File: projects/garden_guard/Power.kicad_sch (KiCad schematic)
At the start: 46 parts, among them IC1 ACPL-227-50CE, IC2 INA226AQDGSRQ1, IC3 INA226AQDGSRQ1, J8 USB_C_Receptacle_USB2.0, U7 Ag5810, U8 TPS2121RUXR, U9 MAX20408AFOF

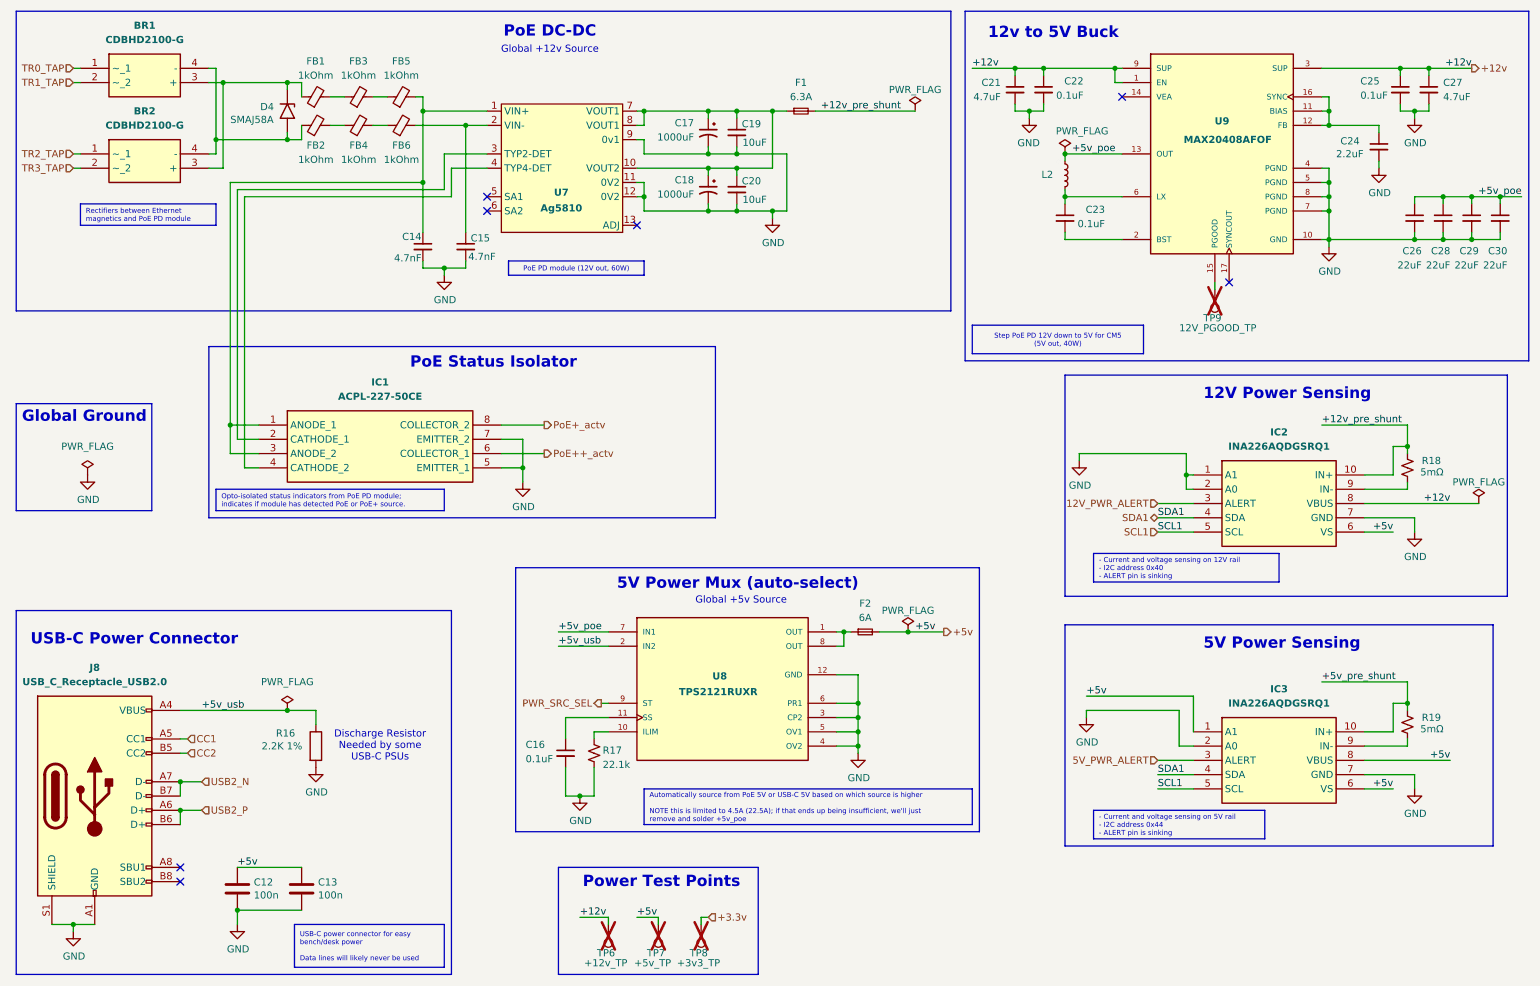
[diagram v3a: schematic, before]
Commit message: - Find part numbers for CM5 parts - Minor CM5 symbol, footprint adjustments - Move to uniform small resistor and capacitor symbols - Add *lck to .gitignore
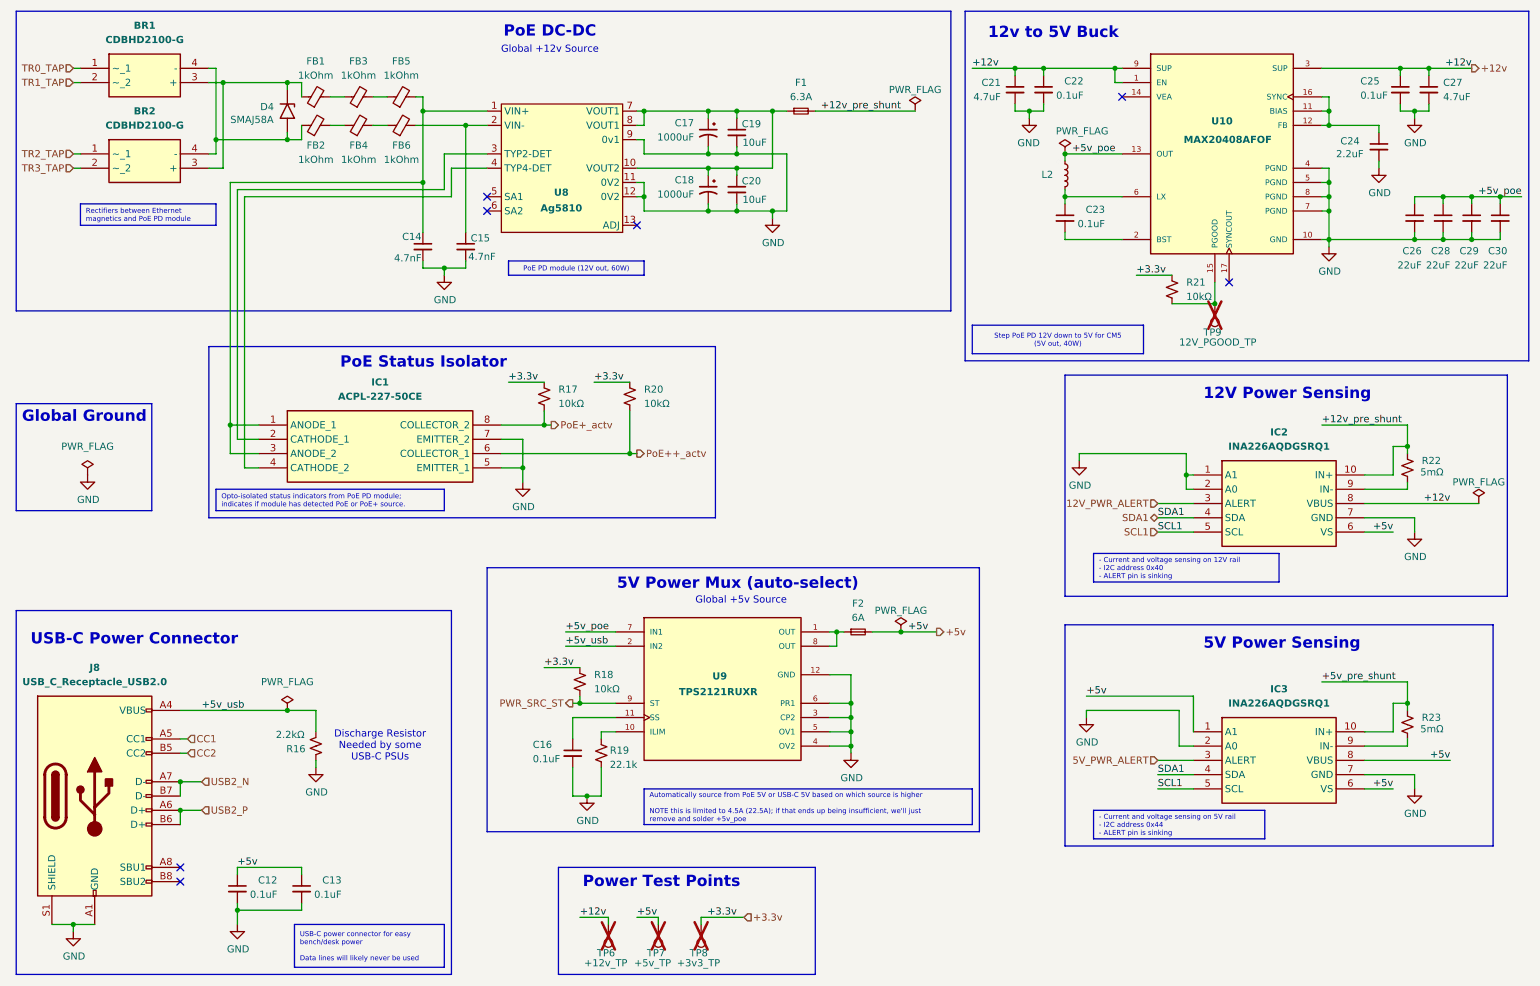
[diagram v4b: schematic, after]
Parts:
- removed C12, C13: 100n, Capacitor_SMD:C_0402_1005Metric, symbol Device:C
- removed R16: 2.2K 1%, Resistor_SMD:R_0402_1005Metric, symbol Device:R
- added C12, C13: 0.1uF, Resistor_SMD:R_0603_1608Metric, symbol Device:C_Small
- added R16: 2.2kΩ, Resistor_SMD:R_0201_0603Metric, symbol Device:R_Small_US
- added R17, R18, R20, R21: 10kΩ, Resistor_SMD:R_0603_1608Metric, symbol Device:R_Small_US
- BR1, BR2: MPN (none) -> CDBHD2100-G; Mfr (none) -> Comchip Technology
- C16, C22, C23, C25: Mfr (none) -> KEMET
- IC1: MPN (none) -> ACPL-227-50CE; Mfr (none) -> Broadcom Limited
- IC2, IC3: MPN (none) -> INA226AQDGSRQ1; Mfr (none) -> Texas Instruments
- J8: MPN (none) -> UJ20-C-H-G-SMT-1-P16-TR; Mfr (none) -> Same Sky
- U10: renamed from U9; MPN (none) -> MAX20408AFOF/VY+; Mfr (none) -> Analog Devices
- U8: renamed from U7; MPN (none) -> AG5810; Mfr (none) -> Silvertel
- U9: renamed from U8; MPN (none) -> TPS2121RUXR; Mfr (none) -> Texas Instruments
- renumbered R17 to R19, R18 to R22, R19 to R23
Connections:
- net +3.3v: now also R17.1, R18.1, R20.1, R21.1
- net +5v: now also C12.1, C13.1
- net +5v_usb: now also R16.1
- net GND: now also C12.2, C13.2, R16.2
- net PoE++_actv: now also R20.2
- net PoE+_actv: now also R17.2
- net at TP9.1, U10.15 (PGOOD): now also R21.2
- net PWR_SRC_SEL renamed PWR_SRC_ST
- net PWR_SRC_ST: now also R18.2
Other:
- moved on the sheet: C16, F2, R19, TP9

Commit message: - Assign 3D models to lingering footprints lacking them - Start playing with board layout - Move CM5 library files from project to components dir
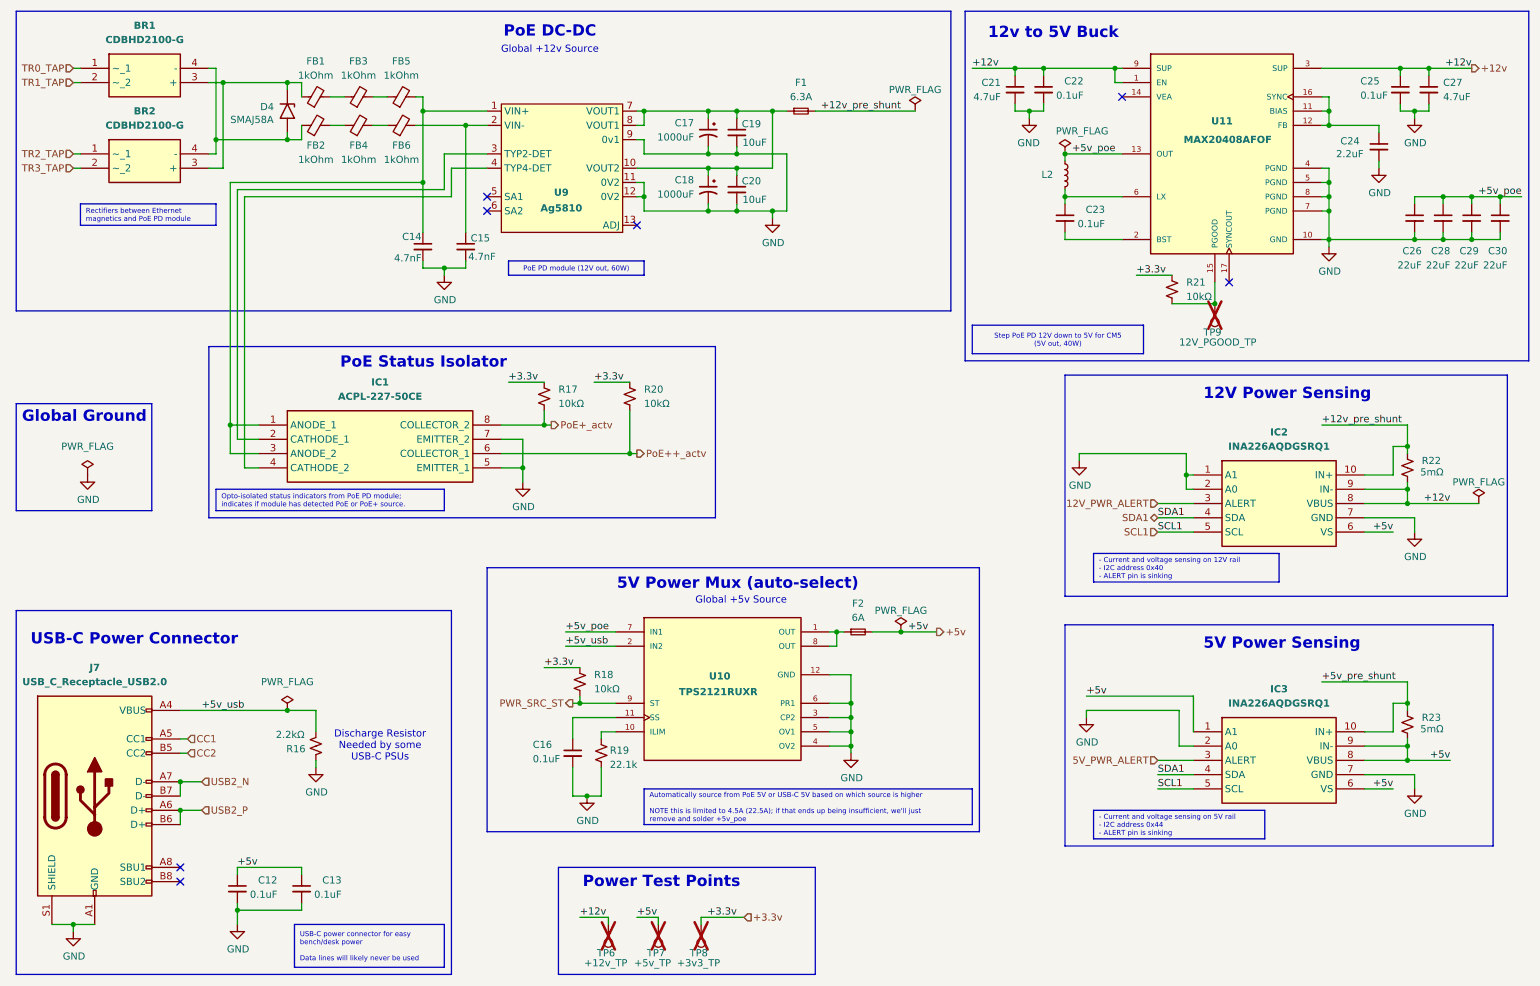
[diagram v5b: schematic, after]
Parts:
- IC1: footprint Custom_PoE:SOIC127P700X220-8N -> Custom_PoE:ACPL-227-50CE
- renumbered J8 to J7, U9 to U10, U10 to U11, U8 to U9
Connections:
- net +12v: now also IC2.9 (IN-), R22.2
- net +5v: now also IC3.9 (IN-), R23.2
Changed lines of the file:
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@@
 	)
 	(junction
+		(at 261.62 144.78)
+		(diameter 0)
+		(color 0 0 0 0)
+	)
+	(junction
 		(at 86.36 31.75)
 		(diameter 0)
@@
 	)
 	(junction
+		(at 261.62 99.06)
+		(diameter 0)
+		(color 0 0 0 0)
+	)
+	(junction
 		(at 260.35 24.13)
 		(diameter 0)
@@
 	)
 	(junction
+		(at 261.62 101.6)
+		(diameter 0)
+		(color 0 0 0 0)
+	)
+	(junction
 		(at 24.13 176.53)
 		(diameter 0)
@@
 	)
 	(junction
+		(at 261.62 147.32)
+		(diameter 0)
+		(color 0 0 0 0)
+	)
+	(junction
 		(at 261.62 137.16)
 		(diameter 0)
@@
 	(wire
 		(pts
+			(xy 261.62 99.06) (xy 261.62 101.6)
+		)
+		(stroke
+			(width 0)
+			(type default)
+		)
+	)
+	(wire
+		(pts
 			(xy 267.97 46.99) (xy 267.97 48.26)
 		)
@@
 	(wire
 		(pts
-			(xy 254 101.6) (xy 274.32 101.6)
+			(xy 254 101.6) (xy 261.62 101.6)
 		)
 		(stroke
@@
 	(wire
 		(pts
+			(xy 261.62 101.6) (xy 274.32 101.6)
+		)
+		(stroke
+			(width 0)
+			(type default)
+		)
+	)
+	(wire
+		(pts
 			(xy 49.53 36.83) (xy 62.23 36.83)
 		)
@@
 	(wire
 		(pts
+			(xy 261.62 144.78) (xy 261.62 147.32)
+		)
+		(stroke
+			(width 0)
+			(type default)
+		)
+	)
+	(wire
+		(pts
 			(xy 166.37 124.46) (xy 171.45 124.46)
 		)
@@
 	(wire
 		(pts
-			(xy 254 147.32) (xy 269.24 147.32)
+			(xy 254 147.32) (xy 261.62 147.32)
 		)
 		(stroke
@@
 	(wire
 		(pts
+			(xy 261.62 147.32) (xy 269.24 147.32)
+		)
+		(stroke
+			(width 0)
+			(type default)
+		)
+	)
+	(wire
+		(pts
 			(xy 158.75 139.7) (xy 162.56 139.7)
 		)
@@
 			)
 		)
-		(property "Footprint" "Custom_PoE:SOIC127P700X220-8N"
+		(property "Footprint" "Custom_PoE:ACPL-227-50CE"
 			(at 96.52 182.55 0)
 			(effects
@@
 		(on_board yes)
 		(dnp no)
-		(property "Reference" "U10"
+		(property "Reference" "U11"
 			(at 228.6 33.528 0)
 			(effects
@@
 			(project ""
 				(path "/dcdac9d4-ef08-426f-b97c-7b9219501e71/446b5b12-2582-472d-9a1e-c1c7d43f42d1"
-					(reference "U10")
+					(reference "U11")
 					(unit 1)
 				)
@@
 		(on_board yes)
 		(dnp no)
-		(property "Reference" "U8"
+		(property "Reference" "U9"
 			(at 110.998 46.228 0)
 			(effects
@@
 			(project ""
 				(path "/dcdac9d4-ef08-426f-b97c-7b9219501e71/446b5b12-2582-472d-9a1e-c1c7d43f42d1"
-					(reference "U8")
+					(reference "U9")
 					(unit 1)
 				)
@@
 		(dnp no)
 		(fields_autoplaced yes)
-		(property "Reference" "J8"
+		(property "Reference" "J7"
 			(at 27.94 130.81 0)
 			(effects
@@
 			(project "garden_guard"
 				(path "/dcdac9d4-ef08-426f-b97c-7b9219501e71/446b5b12-2582-472d-9a1e-c1c7d43f42d1"
-					(reference "J8")
+					(reference "J7")
 					(unit 1)
 				)
@@
 		(on_board yes)
 		(dnp no)
-		(property "Reference" "U9"
+		(property "Reference" "U10"
 			(at 139.192 132.334 0)
 			(effects
@@
 			(project ""
 				(path "/dcdac9d4-ef08-426f-b97c-7b9219501e71/446b5b12-2582-472d-9a1e-c1c7d43f42d1"
-					(reference "U9")
+					(reference "U10")
 					(unit 1)
 				)

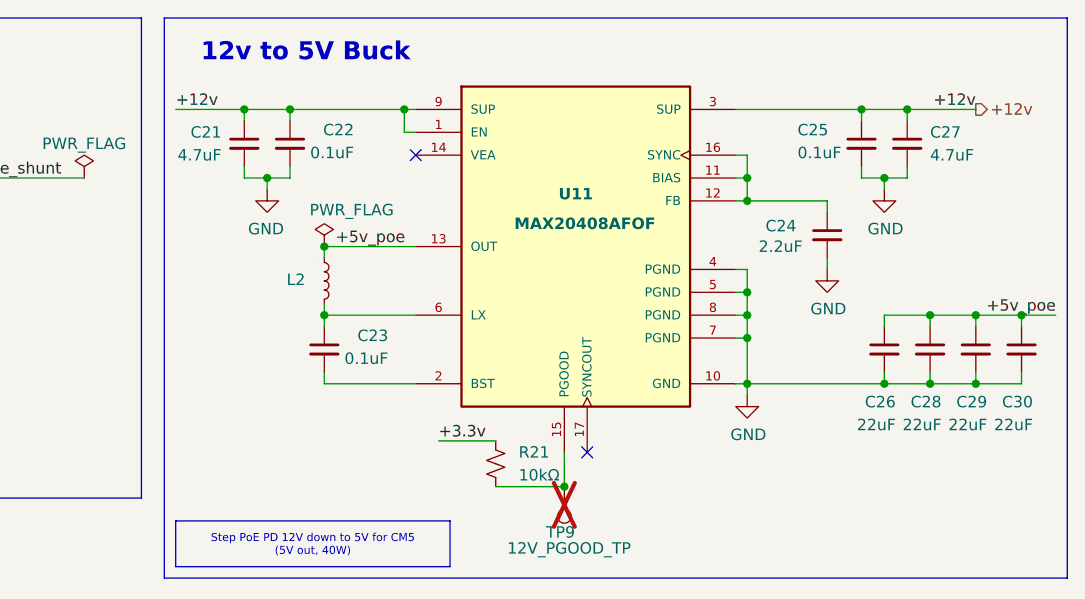
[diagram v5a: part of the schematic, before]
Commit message: 12V to 5V buck converter layout
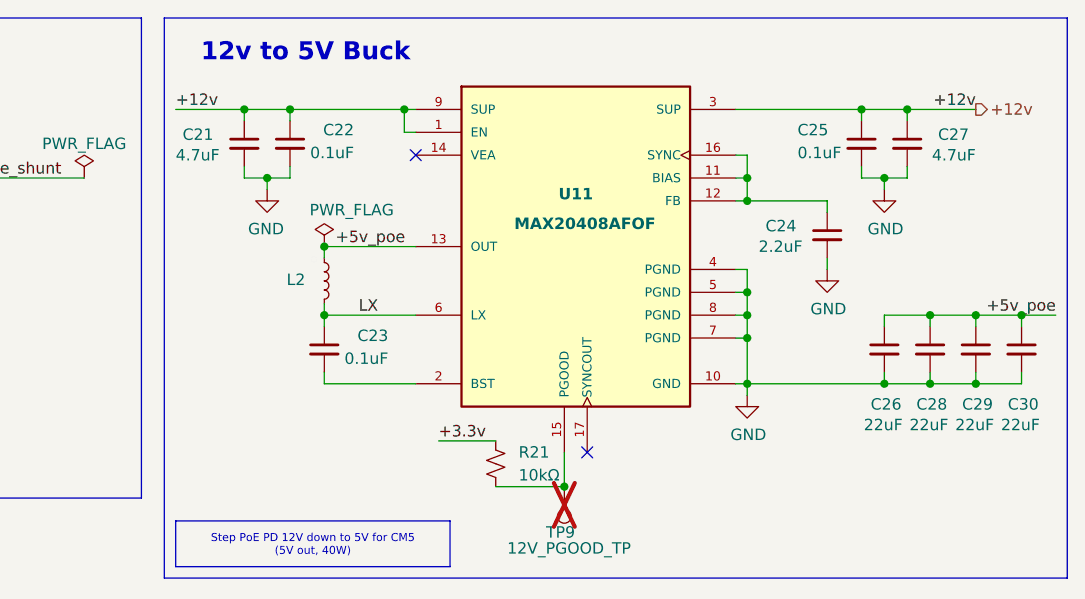
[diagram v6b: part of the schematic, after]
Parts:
- C21, C27: footprint Capacitor_SMD:C_0603_1608Metric -> Capacitor_SMD:C_0805_2012Metric; MPN GRM188R61E475KE11D -> GRM21BZ71E475KE15L; Max Temp (none) -> 125; Rating (none) -> None; Temp Coef (none) -> X7R; Tolerance (none) -> 10%; Voltage (none) -> 25V
- C22, C25: footprint Resistor_SMD:R_0603_1608Metric -> Capacitor_SMD:C_0603_1608Metric
- C24: footprint Capacitor_SMD:C_0201_0603Metric -> Capacitor_SMD:C_0603_1608Metric
- C26, C28, C29, C30: footprint Capacitor_SMD:C_0603_1608Metric -> Capacitor_SMD:C_0805_2012Metric; MPN GRM21BR61E226ME44L -> GRM219R71E224KA01D; Max Temp (none) -> 125; Rating (none) -> None; Temp Coef (none) -> X7R; Tolerance (none) -> 10%; Voltage (none) -> 25V
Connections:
- net LX: now reaches C23.1, L2.2, U11.6 (LX)

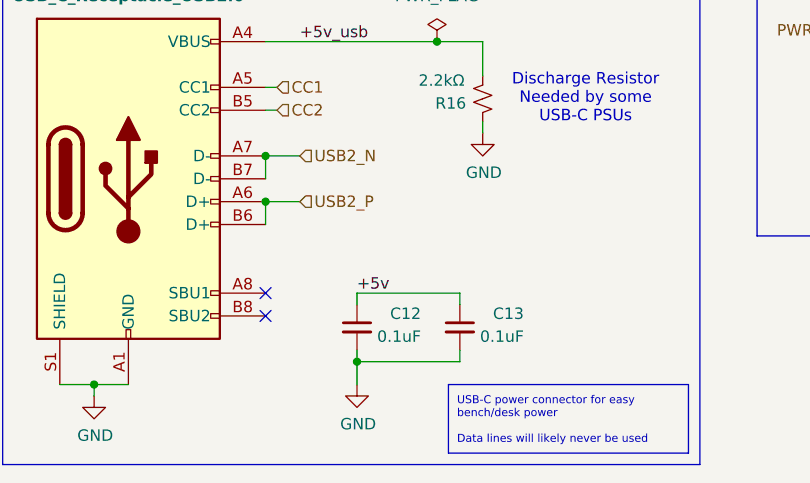
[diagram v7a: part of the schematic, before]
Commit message: - Replace micro HDMI with mini HDMI - Start arrangement of sub-layouts
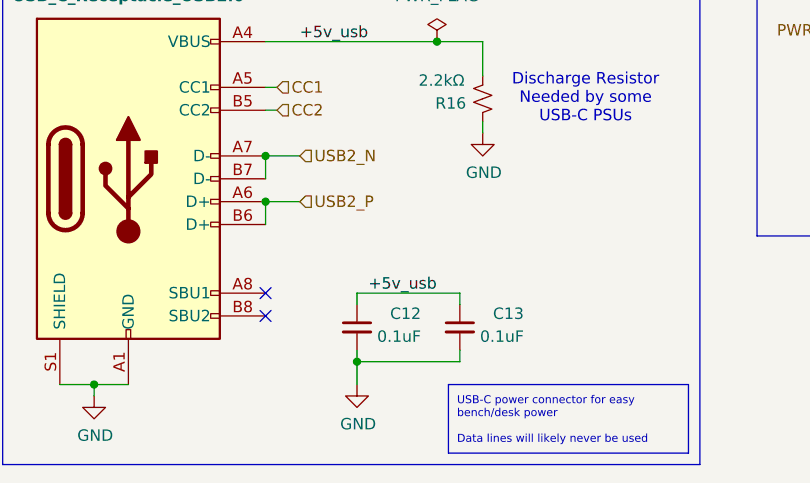
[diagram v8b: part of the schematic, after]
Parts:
- R16: footprint Resistor_SMD:R_0201_0603Metric -> Resistor_SMD:R_0603_1608Metric
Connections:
- net +5v: no longer C12.1, C13.1
- net +5v_usb: now also C12.1, C13.1
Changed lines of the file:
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@@
 		)
 	)
+	(label "+5v_usb"
+		(at 54.61 166.37 0)
+		(effects
+			(font
+				(size 1.27 1.27)
+			)
+			(justify left bottom)
+		)
+	)
 	(label "+5v"
 		(at 172.72 124.46 0)
@@
 		)
 	)
-	(label "+5v"
-		(at 53.34 166.37 0)
-		(effects
-			(font
-				(size 1.27 1.27)
-			)
-			(justify left bottom)
-		)
-	)
 	(label "+5v_usb"
 		(at 46.99 138.43 0)
@@
 			)
 		)
-		(property "Footprint" "Resistor_SMD:R_0201_0603Metric"
+		(property "Footprint" "Resistor_SMD:R_0603_1608Metric"
 			(at 67.31 144.78 0)
 			(effects
